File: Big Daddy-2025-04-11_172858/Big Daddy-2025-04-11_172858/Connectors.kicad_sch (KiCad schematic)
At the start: 7 parts, among them J10 Conn_01x02, J11 Conn_01x23, J12 Conn_01x14, J13 Conn_01x14, J15 Conn_01x02, J8 Conn_01x14, J9 Conn_01x08

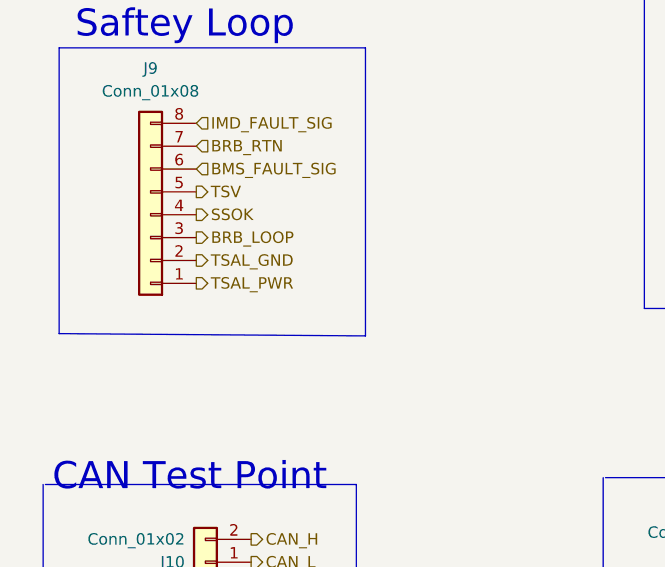
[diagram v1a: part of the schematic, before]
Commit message: changed LED connections and logic
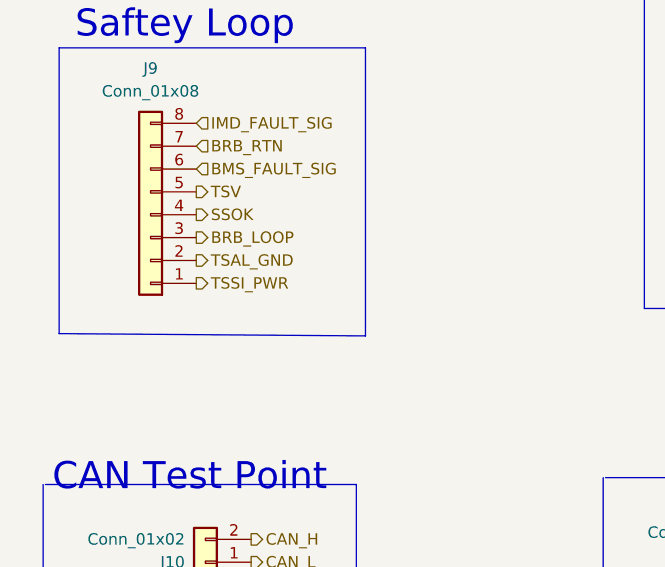
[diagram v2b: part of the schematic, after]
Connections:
- net TSAL_PWR renamed TSSI_PWR
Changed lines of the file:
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@@
 		)
 	)
-	(hierarchical_label "TSAL_PWR"
+	(hierarchical_label "TSSI_PWR"
 		(shape output)
 		(at 46.228 134.366 0)

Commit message: all the bs
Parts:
- removed J9: Conn_01x08, AERO_Footprints:TE_1-776280-1_8pin_Horizontal, symbol Connector_Generic:Conn_01x08
- added J17: Conn_01x14, AERO_Footprints:TE_1-776266-1_14pin_Horizontal, symbol Connector_Generic:Conn_01x14
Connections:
- net BMS_FAULT_SIG: now also J17.12 (Pin_12)
- net BRB_LOOP: now also J17.10 (Pin_10)
- net BRB_RTN: now also J17.13 (Pin_13)
- net IMD_FAULT_SIG: now also J17.14 (Pin_14)
- net TSV: now also J17.11 (Pin_11)
- new net TSSI_Green_in: J17.7 (Pin_7)
- new net TSSI_Green_out: J17.6 (Pin_6)
- new net TSSI_Red_in: J17.8 (Pin_8)
- new net TSSI_Red_out: J17.9 (Pin_9)
